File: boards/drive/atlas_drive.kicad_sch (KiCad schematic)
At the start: 0 parts

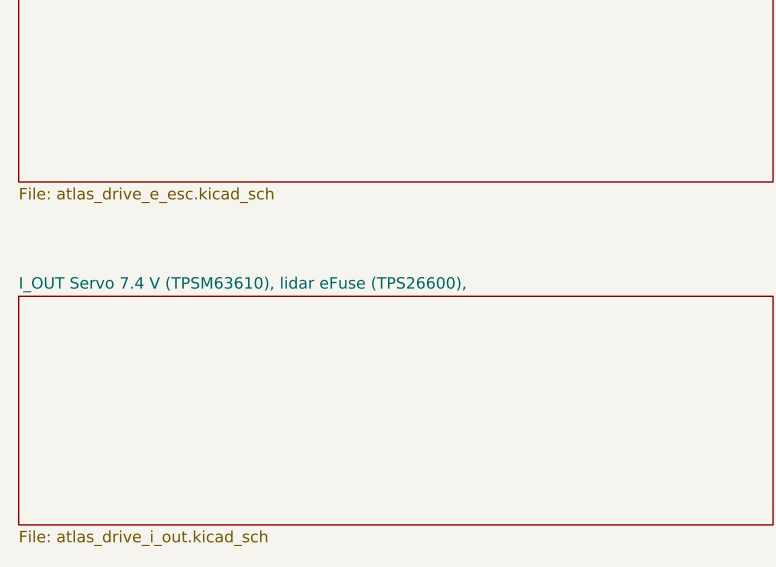
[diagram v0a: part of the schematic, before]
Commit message: Review fixes: docs, run_kicad.sh and drive board text
- README, docs/ARCHITECTURE.md, share/README.md, boards/tools/README.md: status,
  rebuild steps and tool notes brought up to date
- run_kicad.sh: the optional first argument is a sync tarball or an empty string
- Drive schematic text: header J702, 7.5 V servo rail, the precharge resistors
  take 0.15 J each (R319/R320 descriptions synced on the board)
- BOM wording: 7.5 V servo rail

DRC unchanged: no unconnected items, no clearance errors, 8 silkscreen and
track-end warnings.

Co-Authored-By: Claude Opus 5.5 <noreply@anthropic.com>
Claude-Session: https://claude.ai/code/session_01XVBHou86msuHYBGRPr641F
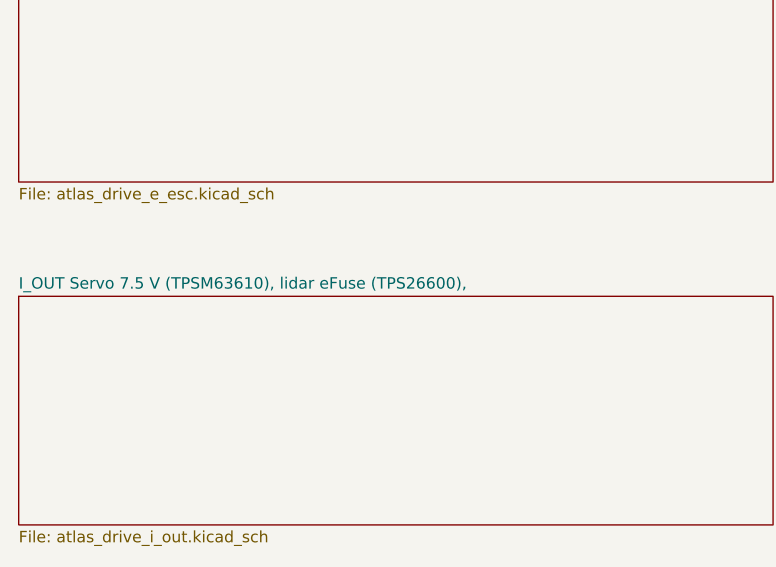
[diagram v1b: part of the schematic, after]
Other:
- sheet I_OUT Servo 7.4 V (TPSM63610), lidar eFuse (TPS26600), renamed I_OUT Servo 7.5 V (TPSM63610), lidar eFuse (TPS26600),
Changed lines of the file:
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@@
  (instances (project "atlas_drive" (path "/aa1fbb69-c53a-5a7c-9e29-d1b48b1ecc80" (page "9")))))
 (sheet (at 25.40 127.00) (size 83.82 25.4) (fields_autoplaced yes) (stroke (width 0.1524) (type solid)) (fill (color 0 0 0 0.0000))
- (property "Sheetname" "I_OUT Servo 7.4 V (TPSM63610), lidar eFuse (TPS26600)," (at 25.40 126.30 0) (effects (font (size 1.27 1.27)) (justify left bottom)))
+ (property "Sheetname" "I_OUT Servo 7.5 V (TPSM63610), lidar eFuse (TPS26600)," (at 25.40 126.30 0) (effects (font (size 1.27 1.27)) (justify left bottom)))
  (property "Sheetfile" "atlas_drive_i_out.kicad_sch" (at 25.40 153.00 0) (effects (font (size 1.27 1.27)) (justify left top)))
  (instances (project "atlas_drive" (path "/aa1fbb69-c53a-5a7c-9e29-d1b48b1ecc80" (page "10")))))
